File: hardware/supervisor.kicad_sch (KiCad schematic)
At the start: 18 parts, among them U5 STM32L4P5RET6, U6 MCP2562-H-SN, Y1 Crystal_GND24

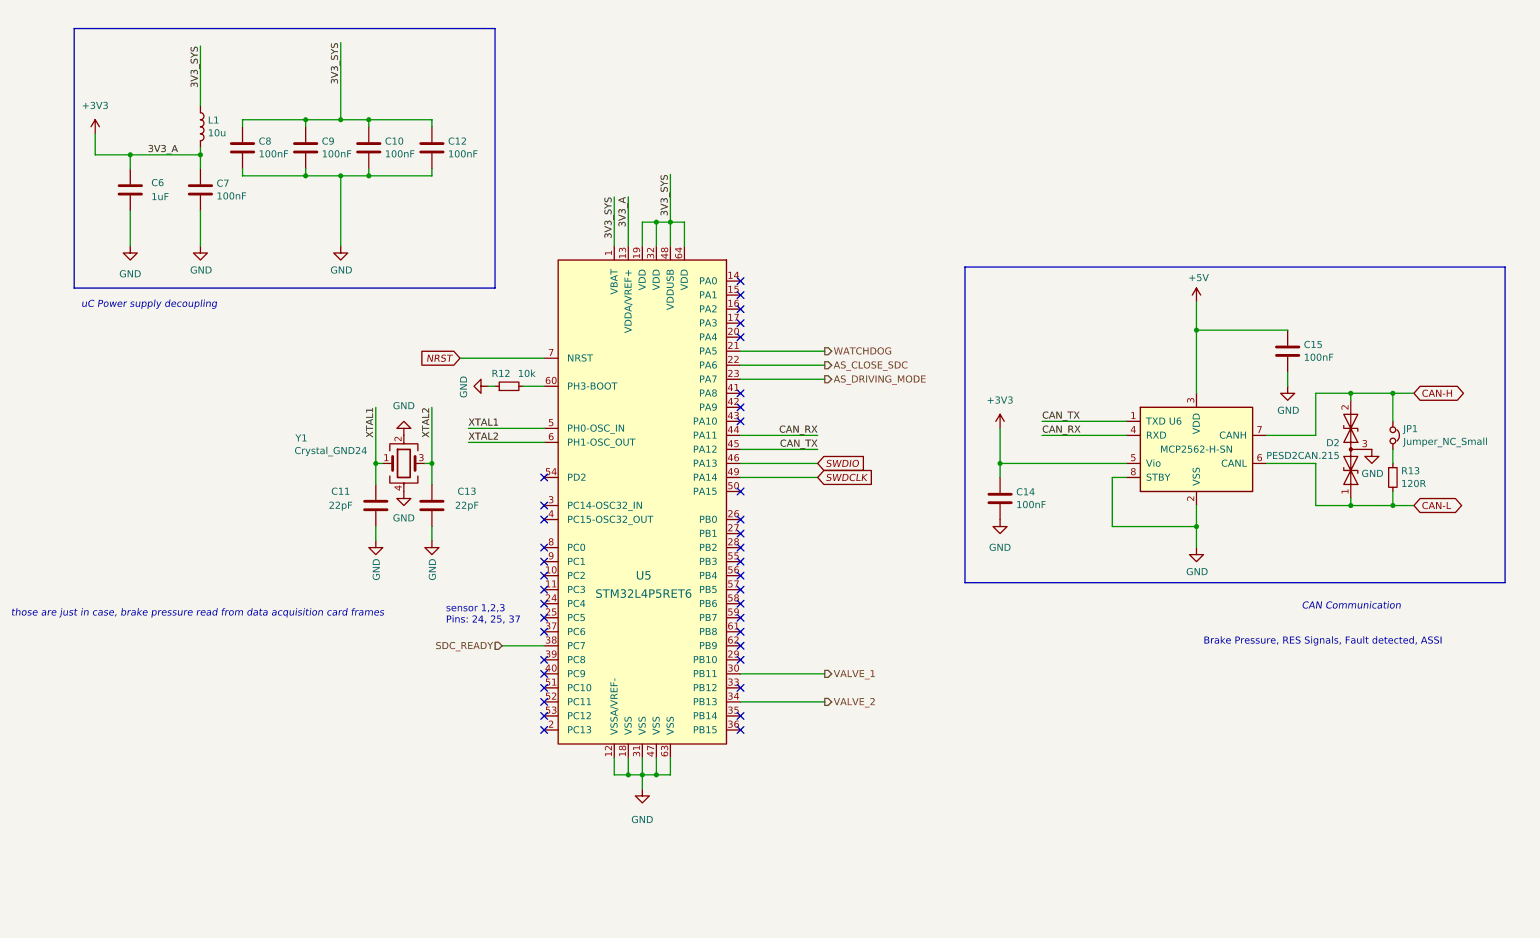
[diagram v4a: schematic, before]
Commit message: 0xERC State
Schematic needs only simulation and veryfying component choice for now
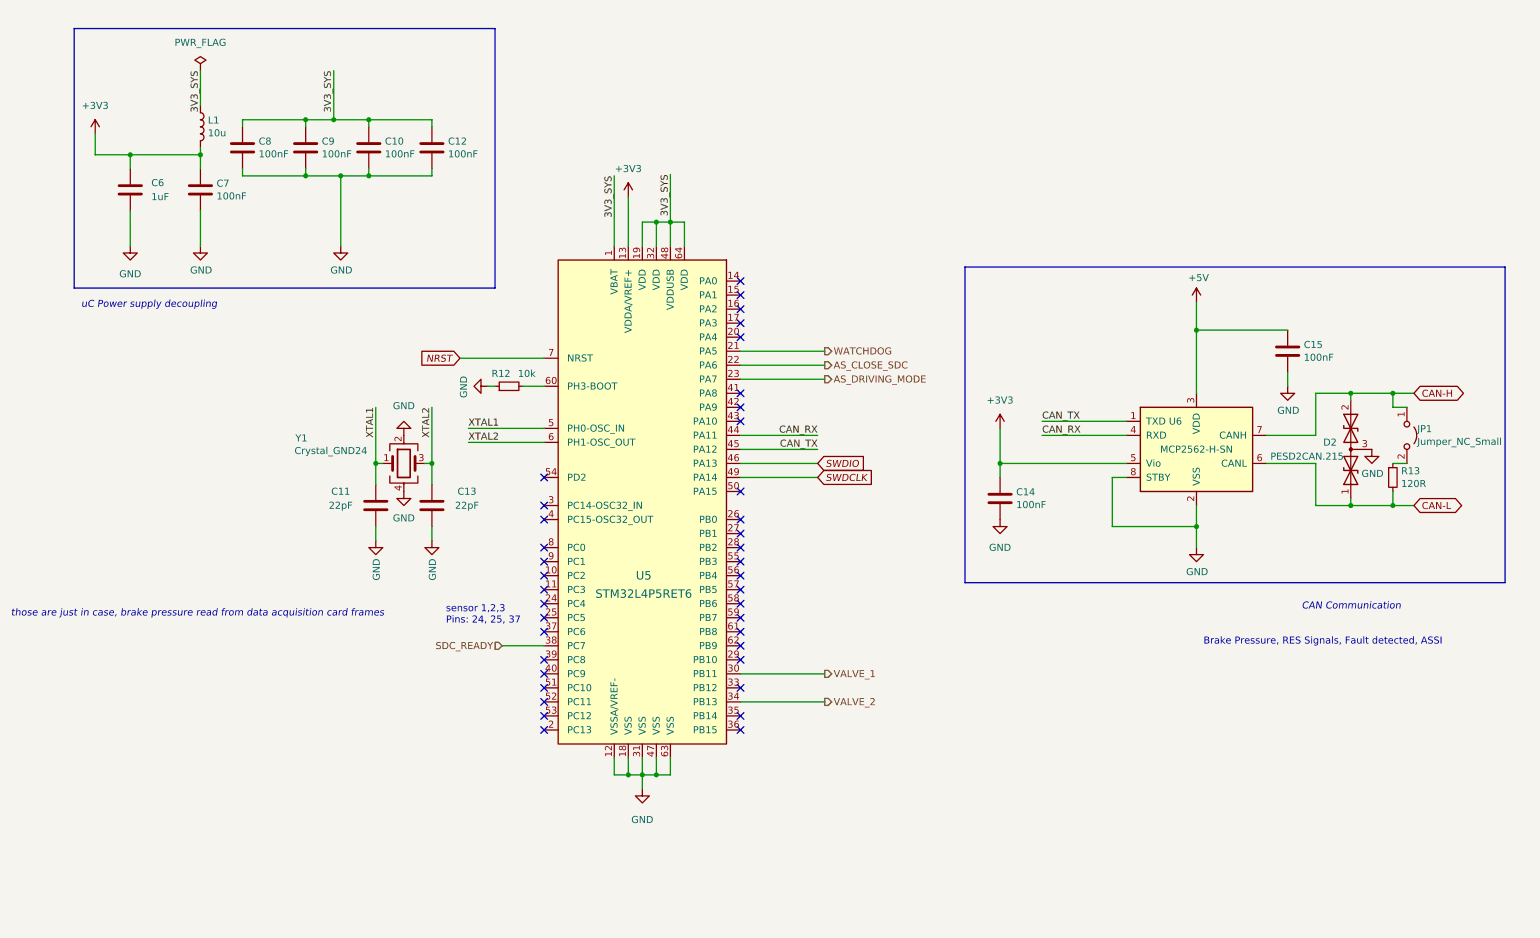
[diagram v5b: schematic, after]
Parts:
- removed D2: PESD2CAN.215, Package_TO_SOT_SMD:SOT-23, symbol Device:D_TVS_x2_AAC
- added D2: PESD2CAN.215, symbol Device:D_TVS_Dual_AAC
- JP1: symbol Device:Jumper_NC_Small -> Jumper:Jumper_2_Open
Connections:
- net CAN-H: now also D2.2 (A2)
- net CAN-L: now also D2.1 (A1)
- net GND: now also D2.3 (common)
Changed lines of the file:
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@@
   (junction (at 191.77 102.87) (diameter 0) (color 0 0 0 0)
   )
+  (junction (at 71.12 40.64) (diameter 0) (color 0 0 0 0)
+  )
   (junction (at 255.27 90.17) (diameter 0) (color 0 0 0 0)
   )
@@
   )
   (junction (at 127 159.258) (diameter 0) (color 0 0 0 0)
-  )
-  (junction (at 72.39 40.64) (diameter 0) (color 0 0 0 0)
   )
   (junction (at 227.33 78.74) (diameter 0) (color 0 0 0 0)
@@
     (stroke (width 0) (type default) (color 0 0 0 0))
   )
-  (wire (pts (xy 262.89 95.25) (xy 262.89 90.17))
+  (wire (pts (xy 262.89 90.17) (xy 262.89 92.71))
     (stroke (width 0) (type default) (color 0 0 0 0))
   )
@@
     (stroke (width 0) (type default) (color 0 0 0 0))
   )
-  (wire (pts (xy 46.99 27.305) (xy 46.99 38.1))
-    (stroke (width 0) (type default) (color 0 0 0 0))
-  )
   (wire (pts (xy 46.99 49.53) (xy 46.99 46.99))
     (stroke (width 0) (type default) (color 0 0 0 0))
@@
     (stroke (width 0) (type default) (color 0 0 0 0))
   )
-  (wire (pts (xy 121.92 54.61) (xy 121.92 63.5))
-    (stroke (width 0) (type default) (color 0 0 0 0))
-  )
   (wire (pts (xy 132.08 59.182) (xy 134.62 59.182))
     (stroke (width 0) (type default) (color 0 0 0 0))
@@
     (stroke (width 0) (type default) (color 0 0 0 0))
   )
+  (wire (pts (xy 71.12 40.64) (xy 77.47 40.64))
+    (stroke (width 0) (type default) (color 0 0 0 0))
+  )
   (wire (pts (xy 214.63 105.41) (xy 212.09 105.41))
     (stroke (width 0) (type default) (color 0 0 0 0))
@@
     (stroke (width 0) (type default) (color 0 0 0 0))
   )
-  (wire (pts (xy 262.89 102.87) (xy 262.89 100.33))
-    (stroke (width 0) (type default) (color 0 0 0 0))
-  )
   (polyline (pts (xy 283.21 67.31) (xy 283.21 124.46))
     (stroke (width 0) (type default) (color 0 0 0 0))
@@
     (stroke (width 0) (type default) (color 0 0 0 0))
   )
-  (wire (pts (xy 77.47 40.64) (xy 72.39 40.64))
-    (stroke (width 0) (type default) (color 0 0 0 0))
-  )
   (wire (pts (xy 243.84 86.36) (xy 243.84 88.9))
     (stroke (width 0) (type default) (color 0 0 0 0))
@@
     (stroke (width 0) (type default) (color 0 0 0 0))
   )
-  (wire (pts (xy 72.39 26.67) (xy 72.39 40.64))
-    (stroke (width 0) (type default) (color 0 0 0 0))
-  )
   (wire (pts (xy 88.9 50.8) (xy 77.47 50.8))
     (stroke (width 0) (type default) (color 0 0 0 0))
@@
     (stroke (width 0) (type default) (color 0 0 0 0))
   )
+  (wire (pts (xy 46.99 38.1) (xy 46.99 31.75))
+    (stroke (width 0) (type default) (color 0 0 0 0))
+  )
   (wire (pts (xy 54.61 50.8) (xy 54.61 49.53))
     (stroke (width 0) (type default) (color 0 0 0 0))
@@
     (stroke (width 0) (type default) (color 0 0 0 0))
   )
+  (wire (pts (xy 265.43 102.87) (xy 262.89 102.87))
+    (stroke (width 0) (type default) (color 0 0 0 0))
+  )
   (wire (pts (xy 88.9 116.84) (xy 88.9 114.3))
     (stroke (width 0) (type default) (color 0 0 0 0))
@@
     (stroke (width 0) (type default) (color 0 0 0 0))
   )
+  (wire (pts (xy 265.43 92.71) (xy 262.89 92.71))
+    (stroke (width 0) (type default) (color 0 0 0 0))
+  )
   (wire (pts (xy 66.04 40.64) (xy 66.04 41.91))
     (stroke (width 0) (type default) (color 0 0 0 0))
@@
     (stroke (width 0) (type default) (color 0 0 0 0))
   )
+  (wire (pts (xy 121.92 50.8) (xy 121.92 63.5))
+    (stroke (width 0) (type default) (color 0 0 0 0))
+  )
   (wire (pts (xy 77.47 40.64) (xy 77.47 41.91))
     (stroke (width 0) (type default) (color 0 0 0 0))
@@
     (stroke (width 0) (type default) (color 0 0 0 0))
   )
+  (wire (pts (xy 71.12 31.75) (xy 71.12 40.64))
+    (stroke (width 0) (type default) (color 0 0 0 0))
+  )
   (polyline (pts (xy 185.42 124.46) (xy 185.42 67.31))
     (stroke (width 0) (type default) (color 0 0 0 0))
@@
     (stroke (width 0) (type default) (color 0 0 0 0))
   )
-  (wire (pts (xy 72.39 40.64) (xy 66.04 40.64))
+  (wire (pts (xy 66.04 40.64) (xy 71.12 40.64))
     (stroke (width 0) (type default) (color 0 0 0 0))
   )
@@
     (effects (font (size 1.27 1.27)) (justify left bottom))
   )
-  (label "3V3_A" (at 124.46 54.61 270)
-    (effects (font (size 1.27 1.27)) (justify right bottom))
-  )
   (label "CAN_TX" (at 158.75 100.33 180)
     (effects (font (size 1.27 1.27)) (justify right bottom))
   )
-  (label "3V3_SYS" (at 121.92 54.61 270)
+  (label "3V3_SYS" (at 121.92 50.8 270)
+    (effects (font (size 1.27 1.27)) (justify right bottom))
+  )
+  (label "3V3_SYS" (at 71.12 31.75 270)
     (effects (font (size 1.27 1.27)) (justify right bottom))
   )
@@
     (effects (font (size 1.27 1.27)) (justify right bottom))
   )
-  (label "3V3_SYS" (at 72.39 26.67 270)
+  (label "3V3_SYS" (at 46.99 31.75 270)
     (effects (font (size 1.27 1.27)) (justify right bottom))
-  )
-  (label "3V3_SYS" (at 46.99 27.305 270)
-    (effects (font (size 1.27 1.27)) (justify right bottom))
-  )
-  (label "3V3_A" (at 37.465 46.99 0)
-    (effects (font (size 1.27 1.27)) (justify left bottom))
   )
   (label "CAN_RX" (at 199.39 97.79 0)
@@
     (pin "2")
   )
+  (symbol (lib_id "power:+3V3") (at 124.46 54.61 0) (unit 1)
+    (in_bom yes) (on_board yes) (fields_autoplaced)
+    (property "Reference" "#PWR0106" (id 0) (at 124.46 58.42 0)
+      (effects (font (size 1.27 1.27)) hide)
+    )
+    (property "Value" "+3V3" (id 1) (at 124.46 49.53 0))
+    (property "Footprint" "" (id 2) (at 124.46 54.61 0)
+      (effects (font (size 1.27 1.27)) hide)
+    )
+    (property "Datasheet" "" (id 3) (at 124.46 54.61 0)
+      (effects (font (size 1.27 1.27)) hide)
+    )
+    (pin "1")
+  )
   (symbol (lib_id "Device:L") (at 46.99 41.91 0) (unit 1)
     (in_bom yes) (on_board yes)
@@
     (pin "1")
     (pin "2")
+  )
+  (symbol (lib_id "power:PWR_FLAG") (at 46.99 31.75 0) (unit 1)
+    (in_bom yes) (on_board yes) (fields_autoplaced)
+    (property "Reference" "#FLG0106" (id 0) (at 46.99 29.845 0)
+      (effects (font (size 1.27 1.27)) hide)
+    )
+    (property "Value" "PWR_FLAG" (id 1) (at 46.99 26.67 0))
+    (property "Footprint" "" (id 2) (at 46.99 31.75 0)
+      (effects (font (size 1.27 1.27)) hide)
+    )
+    (property "Datasheet" "~" (id 3) (at 46.99 31.75 0)
+      (effects (font (size 1.27 1.27)) hide)
+    )
+    (pin "1")
+  )
+  (symbol (lib_id "Device:D_TVS_Dual_AAC") (at 255.27 100.33 90) (unit 1)
+    (in_bom yes) (on_board yes)
+    (property "Reference" "D2" (id 0) (at 252.73 99.0599 90)
+      (effects (font (size 1.27 1.27)) (justify left))
+    )
+    (property "Value" "PESD2CAN.215" (id 1) (at 254 101.6 90)
+      (effects (font (size 1.27 1.27)) (justify left))
+    )
+    (property "Footprint" "" (id 2) (at 255.27 104.14 0)
+      (effects (font (size 1.27 1.27)) hide)
+    )
+    (property "Datasheet" "~" (id 3) (at 255.27 104.14 0)
+      (effects (font (size 1.27 1.27)) hide)
+    )
+    (pin "1")
+    (pin "2")
+    (pin "3")
   )
   (symbol (lib_id "power:GND") (at 191.77 113.03 0) (unit 1)
@@
     (pin "9")
   )
-  (symbol (lib_id "Device:Jumper_NC_Small") (at 262.89 97.79 270) (unit 1)
-    (in_bom yes) (on_board yes)
-    (property "Reference" "JP1" (id 0) (at 264.7696 96.6216 90)
-      (effects (font (size 1.27 1.27)) (justify left))
-    )
-    (property "Value" "Jumper_NC_Small" (id 1) (at 264.7696 98.933 90)
-      (effects (font (size 1.27 1.27)) (justify left))
-    )
-    (property "Footprint" "Connector_PinHeader_2.54mm:PinHeader_1x02_P2.54mm_Vertical" (id 2) (at 262.89 97.79 0)
-      (effects (font (size 1.27 1.27)) hide)
-    )
-    (property "Datasheet" "~" (id 3) (at 262.89 97.79 0)
+  (symbol (lib_id "Jumper:Jumper_2_Open") (at 265.43 97.79 270) (unit 1)
+    (in_bom yes) (on_board yes)
+    (property "Reference" "JP1" (id 0) (at 267.3096 96.6216 90)
+      (effects (font (size 1.27 1.27)) (justify left))
+    )
+    (property "Value" "Jumper_NC_Small" (id 1) (at 267.3096 98.933 90)
+      (effects (font (size 1.27 1.27)) (justify left))
+    )
+    (property "Footprint" "Connector_PinHeader_2.54mm:PinHeader_1x02_P2.54mm_Vertical" (id 2) (at 265.43 97.79 0)
+      (effects (font (size 1.27 1.27)) hide)
+    )
+    (property "Datasheet" "~" (id 3) (at 265.43 97.79 0)
       (effects (font (size 1.27 1.27)) hide)
     )
@@
     (pin "1")
   )
-  (symbol (lib_id "Device:D_TVS_x2_AAC") (at 255.27 100.33 90) (unit 1)
-    (in_bom yes) (on_board yes)
-    (property "Reference" "D2" (id 0) (at 253.2634 99.1616 90)
-      (effects (font (size 1.27 1.27)) (justify left))
-    )
-    (property "Value" "PESD2CAN.215" (id 1) (at 253.2634 101.473 90)
-      (effects (font (size 1.27 1.27)) (justify left))
-    )
-    (property "Footprint" "Package_TO_SOT_SMD:SOT-23" (id 2) (at 255.27 104.14 0)
-      (effects (font (size 1.27 1.27)) hide)
-    )
-    (property "Datasheet" "~" (id 3) (at 255.27 104.14 0)
-      (effects (font (size 1.27 1.27)) hide)
-    )
-    (pin "1")
-    (pin "2")
-    (pin "3")
-  )
   (symbol (lib_id "Device:R_Small") (at 102.87 88.9 90) (unit 1)

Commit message: Last schematic todo changes, mother slander on PCB
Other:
- note added: "8Mhz"
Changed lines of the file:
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@@
   )
   (text "those are just in case, brake pressure read from data acquisition card frames"
-    (at 12.7 130.81 0)
+    (at 29.21 151.13 0)
     (effects (font (size 1.27 1.27) italic) (justify left bottom))
   )
-  (text "sensor 1,2,3\nPins: 24, 25, 37" (at 91.44 132.08 0)
+  (text "sensor 1,2,3\nPins: 24, 25, 37" (at 88.9 147.32 0)
     (effects (font (size 1.27 1.27)) (justify left bottom))
   )
+  (text "8Mhz\n" (at 91.44 104.14 0)
+    (effects (font (size 1.27 1.27)) (justify left bottom))
+  )

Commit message: working simulations, assigned footprints
"nightly" relase
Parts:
- added D16, D17, D18: LED, LED_SMD:LED_0603_1608Metric, symbol Device:LED
- added R2, R34, R35, R36, R37, R4, R5: 2.2k, Resistor_SMD:R_0603_1608Metric, symbol Device:R
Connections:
- net AS_CLOSE_SDC: now also R5.2; no longer U5.22 (PA6)
- net AS_DRIVING_MODE: now also R34.2; no longer U5.23 (PA7)
- net GND: now also R35.2, R36.2, R37.2
- net SDC_READY: now also R2.1; no longer U5.38 (PC7)
- net WATCHDOG: now also R4.2; no longer U5.21 (PA5)
- net AIR_MAIN: now reaches U5.10 (PC2)
- net OK: now reaches U5.14 (PA0)
- net OK: now also D16.2 (A)
- net WARNING: now reaches U5.15 (PA1)
- net WARNING: now also D17.2 (A)
- net ERROR: now reaches U5.16 (PA2)
- net ERROR: now also D18.2 (A)
- net AUX1: now reaches U5.26 (PB0)
- net AUX2: now reaches U5.27 (PB1)
- net AIR_REDUNDANT: now reaches U5.8 (PC0)
- net AIR_EBS: now reaches U5.9 (PC1)
- new net: R34.1, U5.23 (PA7)
- new net: D16.1 (K), R35.1
- new net: R4.1, U5.21 (PA5)
- new net: R5.1, U5.22 (PA6)
- new net: R2.2, U5.38 (PC7)
- new net: D17.1 (K), R36.1
- new net: D18.1 (K), R37.1
- no-connect marks 39 -> 31
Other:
- moved on the sheet: C11, C13, C14, Y1
